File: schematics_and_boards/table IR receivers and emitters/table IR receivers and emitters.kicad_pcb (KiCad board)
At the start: 4 copper layers, 80 x 28.1 mm, 28 parts, among them J1 Conn_Input, J2 Conn_Output, Q1 Q_Photo_NPN, Q2 Q_Photo_NPN, Q3 Q_Photo_NPN, Q4 Q_Photo_NPN, Q5 Q_Photo_NPN, Q6 Q_Photo_NPN, Q7 Q_Photo_NPN, Q8 Q_Photo_NPN, U1 74LV165, U2 74HC595

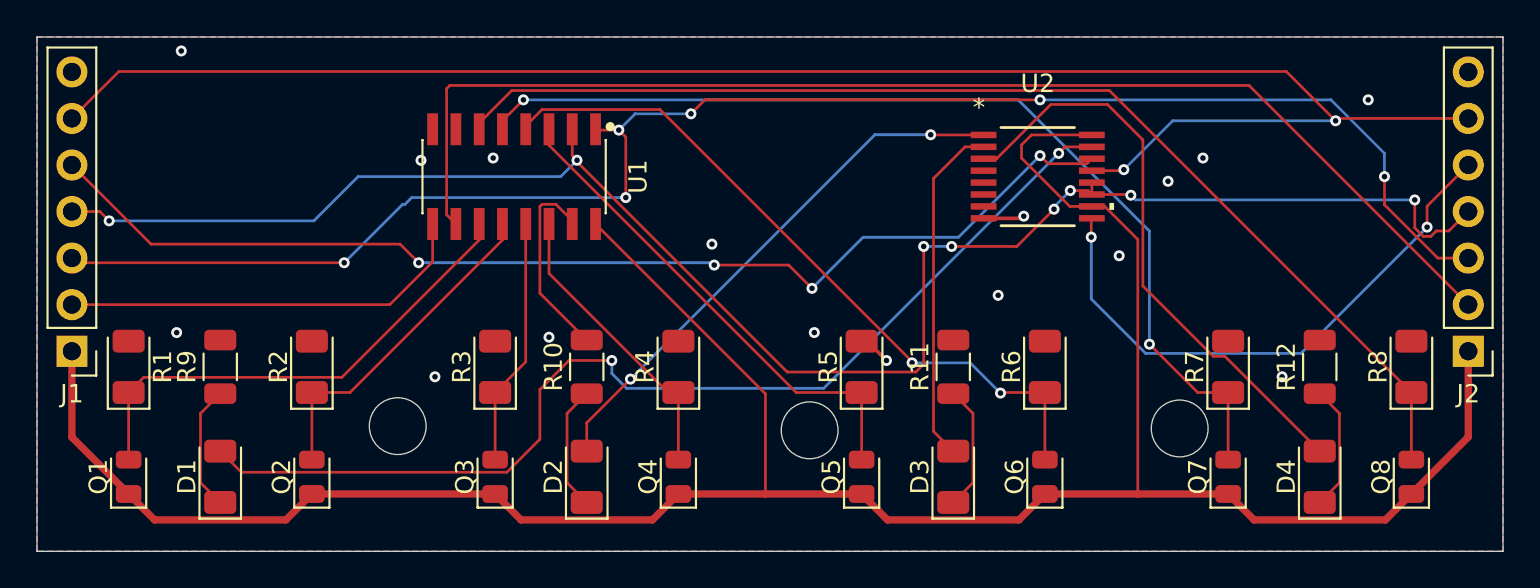
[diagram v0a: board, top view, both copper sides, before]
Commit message: update generic parts to real ones. added decoupling cap. fixed footprints
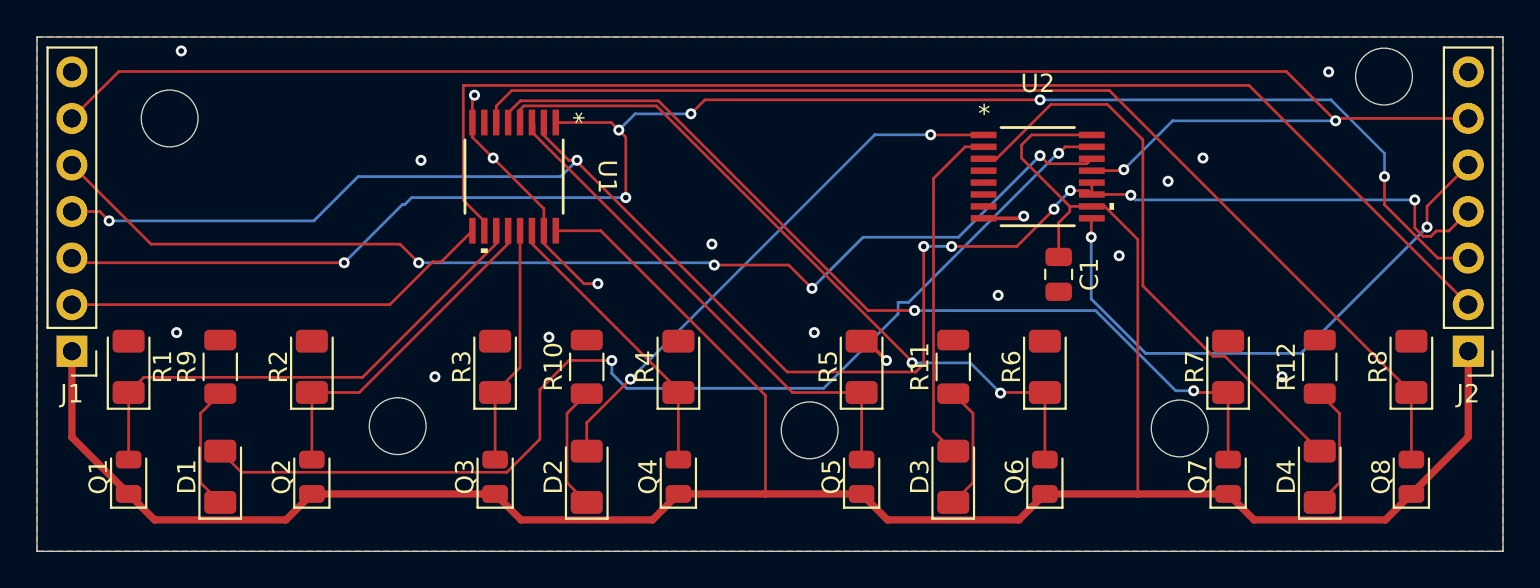
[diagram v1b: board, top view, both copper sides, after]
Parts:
- added C1: 100nF, Capacitor_SMD:C_0805_2012Metric, F.Cu at (156.1, 109.5)
- D1, D2, D3, D4: value LED -> B15W1IR
- Q1, Q2, Q3, Q4, Q5, Q6, Q7, Q8: value Q_Photo_NPN -> B17L1PT
- U1: value 74LV165 -> 74LV165PW-Q100J; footprint Anthony Personal:SOIC127P600X175-16N -> Anthony Personal:TSSOP16_PW_TEX
- U2: value 74HC595 -> SN74HCS595PWR
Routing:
- net VCC: track 138.3 -> 143.2 mm
- net Net-(Q7-E): track 54.4 -> 50.3 mm
- net GND: track 14.7 -> 17.6 mm, vias 16 -> 18
- net Net-(J1-Pin_3): track 89.2 -> 91.5 mm
- net Net-(J1-Pin_4): track 95.5 -> 96.8 mm
- net Net-(J1-Pin_2): track 22.7 -> 23.5 mm
- net Net-(Q8-E): track 62.4 -> 61.7 mm
- net Net-(Q5-E): track 27.2 -> 27.9 mm
- net Net-(Q1-E): track 27.1 -> 27.8 mm
- net Net-(Q6-E): track 39.0 -> 39.6 mm
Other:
- outline, holes or cut-outs redrawn

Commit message: added pcb for mini base
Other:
- copper layers 4 -> 2
- board text added: "D&D Table IR Receiver/Emitter V1"
- board text added: "JLCJLCJLCJLC"
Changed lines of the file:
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@@
 (kicad_pcb (version 20221018) (generator pcbnew)
   (general
-    (thickness 1.6002)
+    (thickness 1.6)
   )
   (paper "USLetter")
@@
   (layers
     (0 "F.Cu" signal "Front")
-    (1 "In1.Cu" signal)
-    (2 "In2.Cu" signal)
     (31 "B.Cu" signal "Back")
     (34 "B.Paste" user)
@@
   )
   (setup
+    (stackup
+      (layer "F.SilkS" (type "Top Silk Screen"))
+      (layer "F.Paste" (type "Top Solder Paste"))
+      (layer "F.Mask" (type "Top Solder Mask") (thickness 0.01))
+      (layer "F.Cu" (type "copper") (thickness 0.035))
+      (layer "dielectric 1" (type "core") (thickness 1.51) (material "FR4") (epsilon_r 4.5) (loss_tangent 0.02))
+      (layer "B.Cu" (type "copper") (thickness 0.035))
+      (layer "B.Mask" (type "Bottom Solder Mask") (thickness 0.01))
+      (layer "B.Paste" (type "Bottom Solder Paste"))
+      (layer "B.SilkS" (type "Bottom Silk Screen"))
+      (copper_finish "None")
+      (dielectric_constraints no)
+    )
     (pad_to_mask_clearance 0)
-    (solder_mask_min_width 0.12)
     (pcbplotparams
       (layerselection 0x00010fc_ffffffff)
@@
     (fp_line (start 1.6 0.8) (end -1.6 0.8)
       (stroke (width 0.1) (type solid)) (layer "F.Fab"))
-    (pad "1" smd roundrect (at -1.4625 0 90) (size 1.125 1.75) (layers "F.Cu" "F.Paste" "F.Mask") (roundrect_rratio 0.222222)
+    (pad "1" smd roundrect (at -1.4625 0 90) (size 1.125 1.75) (layers "F.Cu" "F.Paste" "F.Mask") (roundrect_rratio 0.2222222222)
       (net 6 "Net-(D3-K)") (pintype "passive"))
-    (pad "2" smd roundrect (at 1.4625 0 90) (size 1.125 1.75) (layers "F.Cu" "F.Paste" "F.Mask") (roundrect_rratio 0.222222)
+    (pad "2" smd roundrect (at 1.4625 0 90) (size 1.125 1.75) (layers "F.Cu" "F.Paste" "F.Mask") (roundrect_rratio 0.2222222222)
       (net 16 "GND") (pintype "passive"))
     (model "${KICAD6_3DMODEL_DIR}/Resistor_SMD.3dshapes/R_1206_3216Metric.wrl"
@@
     (fp_line (start 1.6 0.8) (end -1.6 0.8)
       (stroke (width 0.1) (type solid)) (layer "F.Fab"))
-    (pad "1" smd roundrect (at -1.4625 0 90) (size 1.125 1.75) (layers "F.Cu" "F.Paste" "F.Mask") (roundrect_rratio 0.222222)
+    (pad "1" smd roundrect (at -1.4625 0 90) (size 1.125 1.75) (layers "F.Cu" "F.Paste" "F.Mask") (roundrect_rratio 0.2222222222)
       (net 4 "Net-(D2-K)") (pintype "passive"))
-    (pad "2" smd roundrect (at 1.4625 0 90) (size 1.125 1.75) (layers "F.Cu" "F.Paste" "F.Mask") (roundrect_rratio 0.222222)
+    (pad "2" smd roundrect (at 1.4625 0 90) (size 1.125 1.75) (layers "F.Cu" "F.Paste" "F.Mask") (roundrect_rratio 0.2222222222)
       (net 16 "GND") (pintype "passive"))
     (model "${KICAD6_3DMODEL_DIR}/Resistor_SMD.3dshapes/R_1206_3216Metric.wrl"
@@
     (fp_line (start 1.6 0.8) (end -1.6 0.8)
       (stroke (width 0.1) (type solid)) (layer "F.Fab"))
-    (pad "1" smd roundrect (at -1.4625 0 90) (size 1.125 1.75) (layers "F.Cu" "F.Paste" "F.Mask") (roundrect_rratio 0.222222)
+    (pad "1" smd roundrect (at -1.4625 0 90) (size 1.125 1.75) (layers "F.Cu" "F.Paste" "F.Mask") (roundrect_rratio 0.2222222222)
       (net 2 "Net-(D1-K)") (pintype "passive"))
-    (pad "2" smd roundrect (at 1.4625 0 90) (size 1.125 1.75) (layers "F.Cu" "F.Paste" "F.Mask") (roundrect_rratio 0.222222)
+    (pad "2" smd roundrect (at 1.4625 0 90) (size 1.125 1.75) (layers "F.Cu" "F.Paste" "F.Mask") (roundrect_rratio 0.2222222222)
       (net 16 "GND") (pintype "passive"))
     (model "${KICAD6_3DMODEL_DIR}/Resistor_SMD.3dshapes/R_1206_3216Metric.wrl"
@@
     (fp_line (start 1.6 0.8) (end -1.6 0.8)
       (stroke (width 0.1) (type solid)) (layer "F.Fab"))
-    (pad "1" smd roundrect (at -1.4625 0 90) (size 1.125 1.75) (layers "F.Cu" "F.Paste" "F.Mask") (roundrect_rratio 0.222222)
+    (pad "1" smd roundrect (at -1.4625 0 90) (size 1.125 1.75) (layers "F.Cu" "F.Paste" "F.Mask") (roundrect_rratio 0.2222222222)
       (net 8 "Net-(D4-K)") (pintype "passive"))
-    (pad "2" smd roundrect (at 1.4625 0 90) (size 1.125 1.75) (layers "F.Cu" "F.Paste" "F.Mask") (roundrect_rratio 0.222222)
+    (pad "2" smd roundrect (at 1.4625 0 90) (size 1.125 1.75) (layers "F.Cu" "F.Paste" "F.Mask") (roundrect_rratio 0.2222222222)
       (net 16 "GND") (pintype "passive"))
     (model "${KICAD6_3DMODEL_DIR}/Resistor_SMD.3dshapes/R_1206_3216Metric.wrl"
@@
   (gr_circle (center 120.015 117.755) (end 121.565 117.755)
     (stroke (width 0.0381) (type default)) (fill none) (layer "Edge.Cuts"))
+  (gr_text "D&D Table IR Receiver/Emitter V1" (at 179.705 123.952) (layer "B.SilkS")
+    (effects (font (size 0.8128 0.8128) (thickness 0.1524) bold) (justify left bottom mirror))
+  )
+  (gr_text "JLCJLCJLCJLC" (at 109.22 123.825) (layer "B.SilkS")
+    (effects (font (size 0.8128 0.8128) (thickness 0.1524) bold) (justify left bottom mirror))
+  )
   (segment (start 109.253 120.843) (end 110.33 121.92) (width 0.15) (layer "F.Cu") (net 2))
   (segment (start 110.33 115.9825) (end 109.253 117.0595) (width 0.15) (layer "F.Cu") (net 2))

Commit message: initial designs for manufacture
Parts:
- moved J2 0.18 mm to (178.3, 113.5)
- moved J1 0.17 mm to (102.3, 113.5)
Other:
- outline, holes or cut-outs redrawn
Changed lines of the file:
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@@
     )
     (pad_to_mask_clearance 0)
+    (grid_origin 100.33 96.52)
     (pcbplotparams
       (layerselection 0x00010fc_ffffffff)
@@
   (net 30 "unconnected-(U2-QH-Pad7)")
   (footprint "Connector_PinHeader_2.54mm:PinHeader_1x07_P2.54mm_Vertical" (layer "F.Cu")
-    (at 102.235 113.665 180)
+    (at 102.33 113.52 180)
     (descr "Through hole straight pin header, 1x07, 2.54mm pitch, single row")
     (tags "Through hole pin header THT 1x07 2.54mm single row")
@@
   )
   (footprint "Connector_PinHeader_2.54mm:PinHeader_1x07_P2.54mm_Vertical" (layer "F.Cu")
-    (at 178.435 113.665 180)
+    (at 178.33 113.52 180)
     (descr "Through hole straight pin header, 1x07, 2.54mm pitch, single row")
     (tags "Through hole pin header THT 1x07 2.54mm single row")
@@
     )
   )
-  (gr_circle (center 162.687 117.882) (end 164.237 117.882)
+  (gr_circle (center 162.687 117.882) (end 164.187 117.882)
     (stroke (width 0.0381) (type default)) (fill none) (layer "Edge.Cuts"))
-  (gr_circle (center 142.494 117.983) (end 144.044 117.983)
+  (gr_circle (center 142.494 117.983) (end 143.994 117.983)
     (stroke (width 0.0381) (type default)) (fill none) (layer "Edge.Cuts"))
-  (gr_circle (center 173.837 98.679) (end 175.387 98.679)
+  (gr_circle (center 173.837 98.679) (end 175.337 98.679)
     (stroke (width 0.0381) (type default)) (fill none) (layer "Edge.Cuts"))
-  (gr_circle (center 107.569 100.965) (end 109.119 100.965)
+  (gr_circle (center 107.569 100.965) (end 109.069 100.965)
     (stroke (width 0.0381) (type default)) (fill none) (layer "Edge.Cuts"))
   (gr_rect (start 100.33 96.52) (end 180.33 124.587)
     (stroke (width 0.0381) (type default)) (fill none) (layer "Edge.Cuts"))
-  (gr_circle (center 120.015 117.755) (end 121.565 117.755)
+  (gr_circle (center 120.015 117.755) (end 121.515 117.755)
     (stroke (width 0.0381) (type default)) (fill none) (layer "Edge.Cuts"))
   (gr_text "D&D Table IR Receiver/Emitter V1" (at 179.705 123.952) (layer "B.SilkS")
